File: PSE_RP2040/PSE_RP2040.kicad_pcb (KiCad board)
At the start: 2 copper layers, 85 x 60 mm, 129 parts, among them IC1 LAN8742A-CZ, IC2 SAM-M8Q-0, J1 USB_B, J2 USB_B_Mini, J3 8P8C_LED, J4 Conn_01x03, J5 Screw_Terminal_01x02, J6 Conn_01x04_Female, Q2 IRLML6402, SW1 SW_Push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

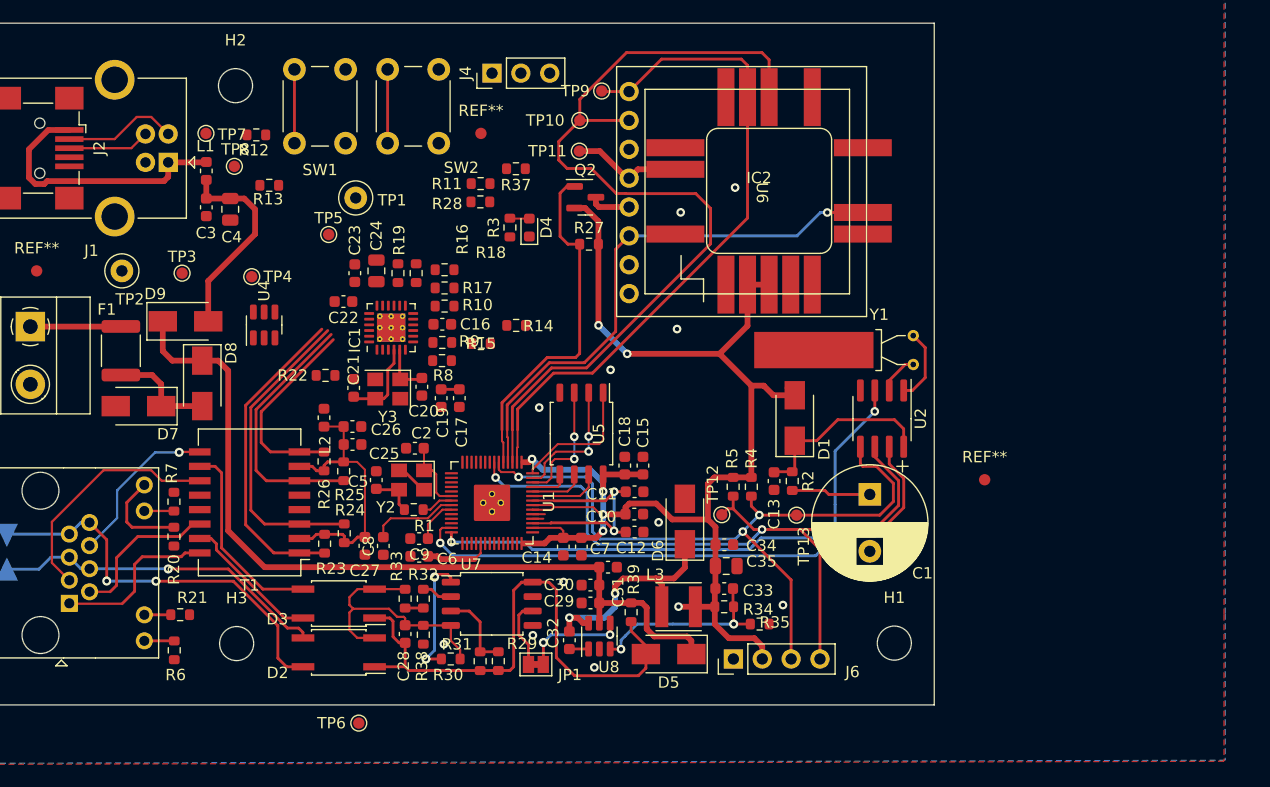
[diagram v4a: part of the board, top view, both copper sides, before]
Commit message: PCB_LAN
corretto alimentazione gps (VDDIO)
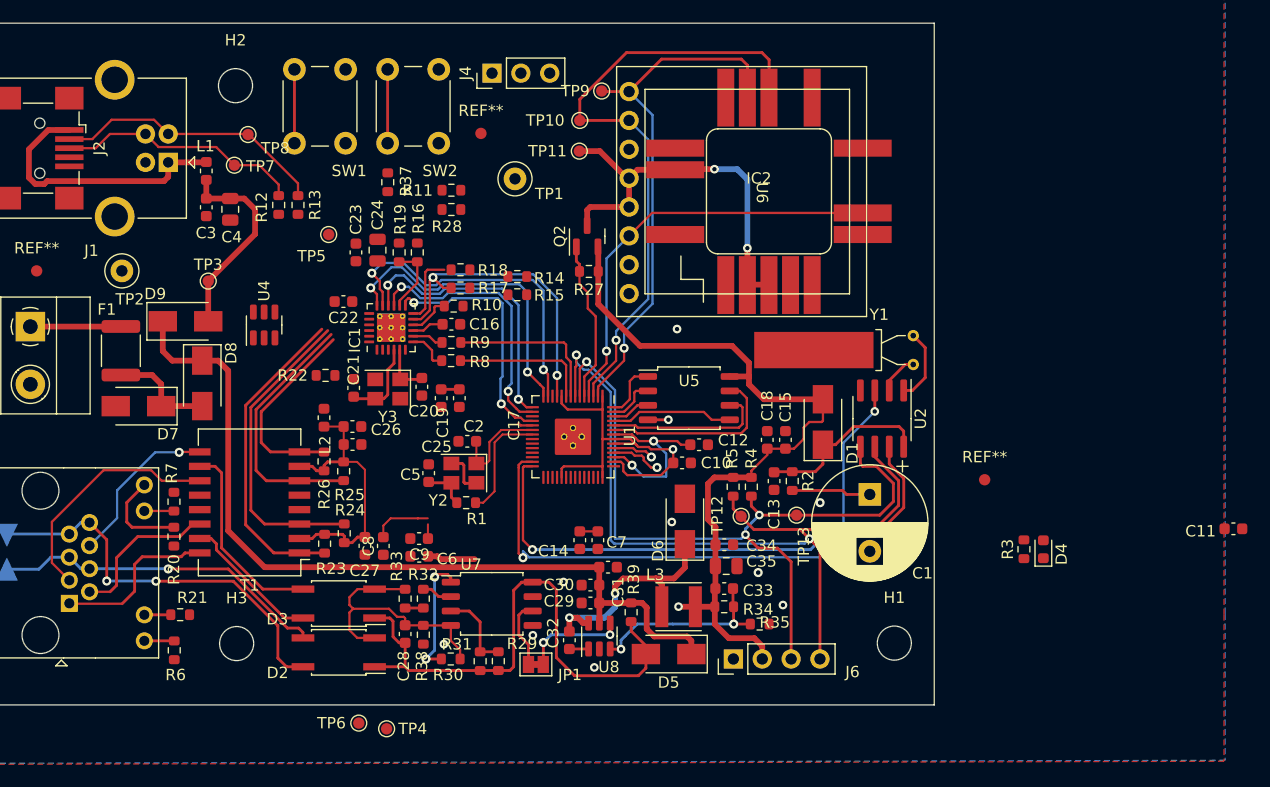
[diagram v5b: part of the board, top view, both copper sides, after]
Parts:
- moved D4 53.4 mm to (194.6, 146.3)
- moved R3 53.4 mm to (192.9, 146.3)
- moved C11 52.8 mm to (211.3, 144.5)
- moved TP4 41.5 mm to (136.8, 162.1)
- moved TP1 14.1 mm to (148.1, 113.7)
- moved C15 12.7 mm to (171.9, 136.7)
- moved C18 12.7 mm to (170.3, 136.7)
- moved R37 11.3 mm to (136.9, 114.0), turned to 90 degrees
- moved U5 9.95 mm to (163.4, 133.0), turned to 0 degrees
- moved C12 9.56 mm to (164.3, 137.1)
- moved U1 9.20 mm to (153.2, 136.4)
- moved R12 6.48 mm to (127.3, 116.0), turned to -90 degrees
- moved C10 6.16 mm to (162.8, 138.7)
- moved R15 5.36 mm to (148.3, 123.9)
- moved C5 4.65 mm to (140.5, 139.6)
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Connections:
- IC2 pad 2: +3V3 -> /VCC_GPS
- IC2 pad 3: +3V3 -> /VCC_GPS
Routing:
- net TXD0: track 0.00 -> 29.6 mm, vias 0 -> 2
- net TXD1: track 0.00 -> 27.3 mm, vias 0 -> 2
- net CRS: track 0.00 -> 27.3 mm, vias 0 -> 2
- net TXEN: track 0.00 -> 25.0 mm, vias 0 -> 2
- net /UART_RX-GPS_TX: track 78.9 -> 55.1 mm, vias 0 -> 1
- net LAN_nRST: track 0.00 -> 23.7 mm, vias 0 -> 2
- net /VCC_GPS: track 13.4 -> 35.4 mm, vias 0 -> 2
- net MDC: track 0.00 -> 21.9 mm, vias 0 -> 2
- net +3V3: track 136.4 -> 115.0 mm, vias 7 -> 2
- net /GPS_EN: track 30.9 -> 14.3 mm
- net /USB_DP: track 7.22 -> 21.8 mm
- net /USB_DN: track 10.1 -> 24.2 mm
- net RXD0: track 0.00 -> 14.0 mm
- net /UART_TX-GPS_RX: track 59.7 -> 46.8 mm, vias 0 -> 1
- net RXD1: track 0.00 -> 12.2 mm
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
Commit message: sbroglio micro
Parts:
- moved C11 47.5 mm to (164.4, 137.1)
- moved TP5 45.7 mm to (132.6, 164.3)
- moved D4 42.3 mm to (152.4, 142.9), turned to 180 degrees
- moved R3 42.1 mm to (150.8, 145.2)
- moved TP4 21.5 mm to (147.0, 143.2)
- moved C9 6.55 mm to (146.2, 145.1)
- moved C12 5.66 mm to (159.7, 140.4)
- moved TP6 4.71 mm to (137.5, 165.1)
- moved C7 1.14 mm to (156.2, 144.7), turned to 0 degrees
- moved C6 1.03 mm to (140.3, 146.1), turned to 90 degrees
- moved U4 0.46 mm to (126.0, 126.1)
- moved R1 0.10 mm to (143.9, 142.2)
- turned REF** to 90 degrees
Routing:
- net /MCU_nRST: track 6.50 -> 57.2 mm, vias 0 -> 3
- net Net-(R12-Pad2): track 3.65 -> 50.4 mm, vias 1 -> 2
- net Net-(R13-Pad2): track 4.50 -> 51.0 mm, vias 1 -> 2
- net /SWDIO: track 0.00 -> 39.9 mm, vias 0 -> 2
- net /SWCLK: track 0.00 -> 38.5 mm, vias 0 -> 2
- net +3V3: track 115.0 -> 152.7 mm, vias 2 -> 1
- net LAN_REFCK: track 0.00 -> 35.8 mm, vias 0 -> 2
- net /QSPI_SS: track 5.08 -> 31.3 mm, vias 0 -> 2
- net +1V1: track 17.3 -> 42.7 mm, vias 2 -> 6
- net MDIO: track 6.21 -> 28.3 mm, vias 0 -> 4
- net Net-(R11-Pad2): track 6.50 -> 21.2 mm
- net Net-(IC1-Pad23): track 22.8 -> 33.6 mm, vias 0 -> 3
- net Net-(IC1-Pad21): track 28.0 -> 38.7 mm, vias 0 -> 2
- net GND: track 7.03 -> 12.7 mm, vias 10 -> 13
- net Net-(IC1-Pad20): track 27.4 -> 31.9 mm
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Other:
- board size 85 x 60 mm -> 85 x 56 mm

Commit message: sbroglio pcb
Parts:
- moved R17 0.50 mm to (142.8, 123.3)
- moved R18 0.50 mm to (142.8, 121.7)
- moved R9 0.20 mm to (142.5, 128.3)
- moved R8 0.15 mm to (142.5, 129.8)
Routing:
- net LEDA_RJ45: track 2.33 -> 34.9 mm, vias 0 -> 2
- net LEDB_RJ45: track 8.24 -> 34.4 mm, vias 0 -> 1
- net Net-(C22-Pad1): track 24.4 -> 49.4 mm
- net +3V3: track 152.7 -> 164.5 mm, vias 1 -> 3
- net Net-(IC1-Pad7): track 3.66 -> 14.6 mm
- net Net-(IC1-Pad8): track 2.77 -> 13.4 mm, vias 0 -> 2
- net Net-(IC1-Pad22): track 20.8 -> 28.8 mm, vias 0 -> 2
- net Net-(IC1-Pad20): track 31.9 -> 39.7 mm
- net Net-(C17-Pad1): track 1.60 -> 7.12 mm
- net Net-(IC1-Pad24): track 0.00 -> 5.04 mm
- net Net-(IC1-Pad23): track 33.6 -> 31.4 mm
- net TXD1: track 27.3 -> 25.2 mm
- net TXEN: track 25.1 -> 23.4 mm
- net TXD0: track 29.9 -> 28.3 mm
- net MDC: track 22.7 -> 21.2 mm
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
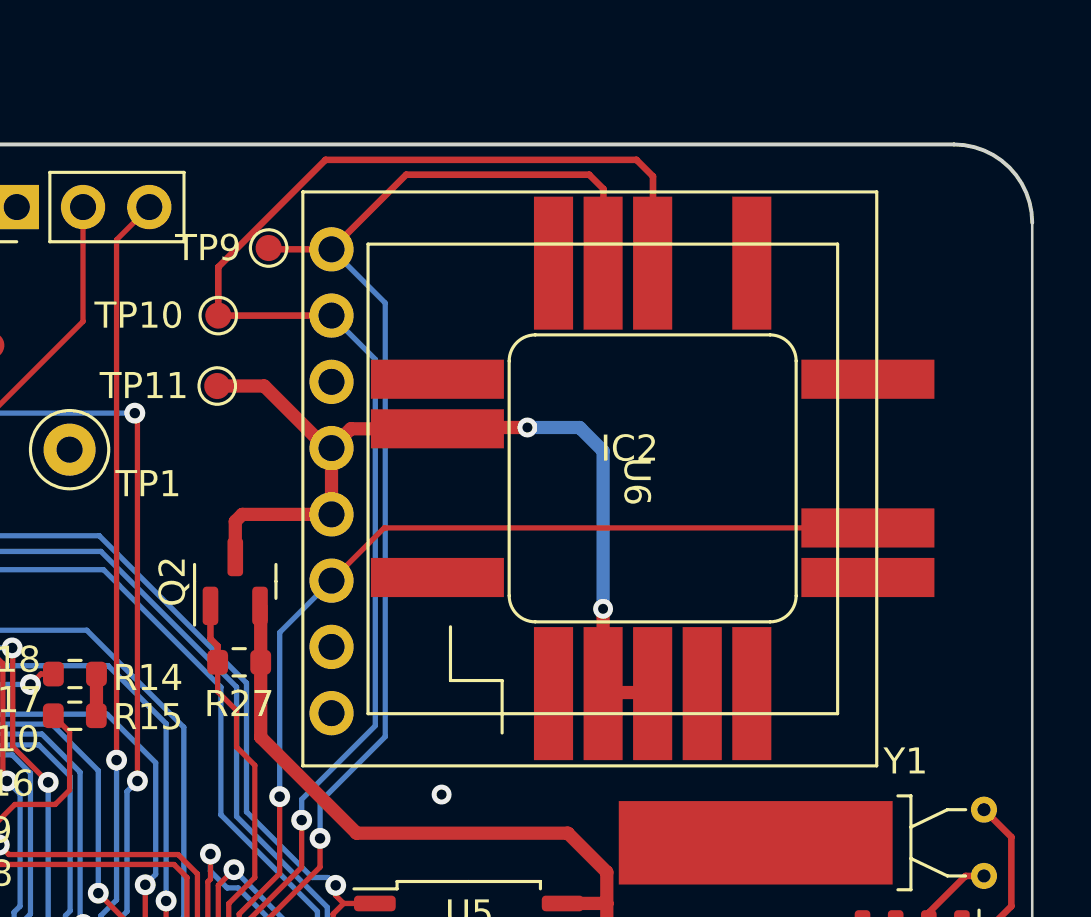
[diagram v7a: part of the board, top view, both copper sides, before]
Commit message: footprint sam8
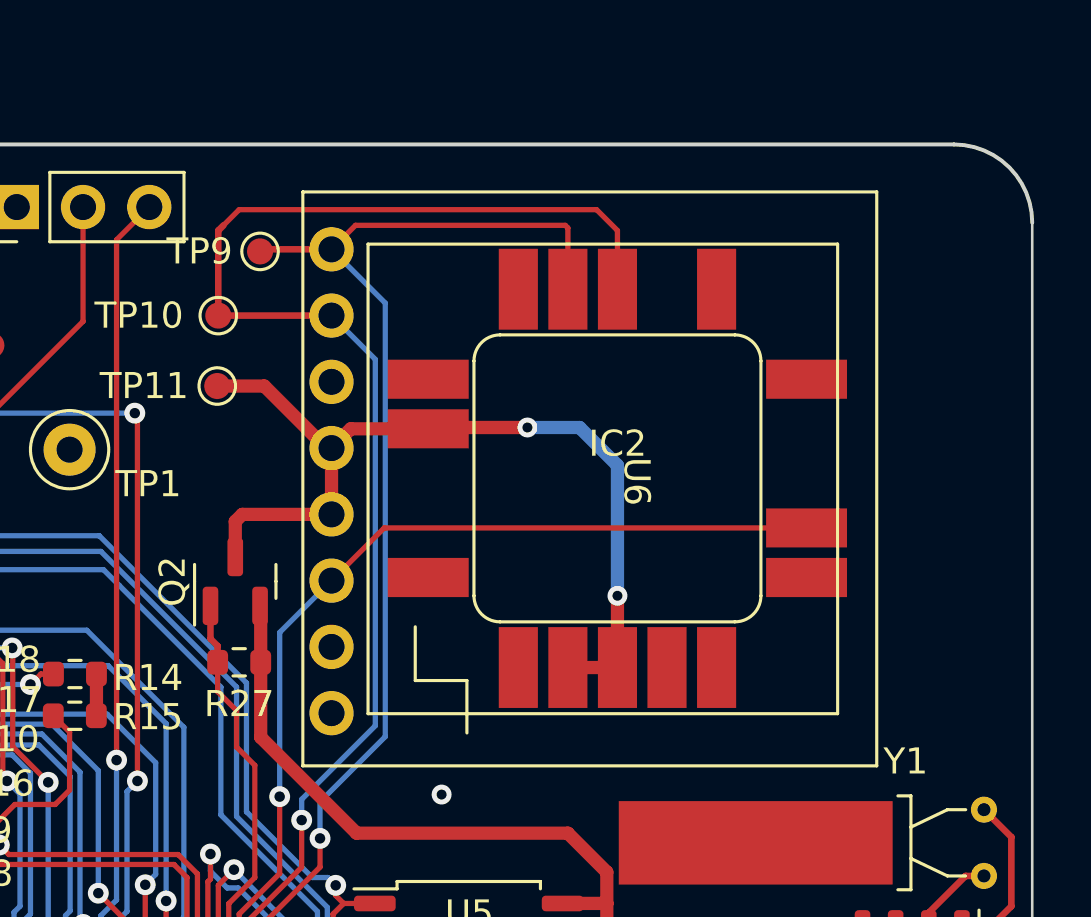
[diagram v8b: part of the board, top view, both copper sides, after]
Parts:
- moved IC2 1.35 mm to (169.1, 114.8)
- moved TP9 0.35 mm to (155.4, 106.1)
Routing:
- net /UART_TX-GPS_RX: track 46.8 -> 44.3 mm
- net /PPS: track 37.0 -> 34.6 mm
- net /UART_RX-GPS_TX: track 55.1 -> 52.8 mm
- net /VCC_GPS: track 35.4 -> 34.6 mm
